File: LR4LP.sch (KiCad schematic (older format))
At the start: 15 parts

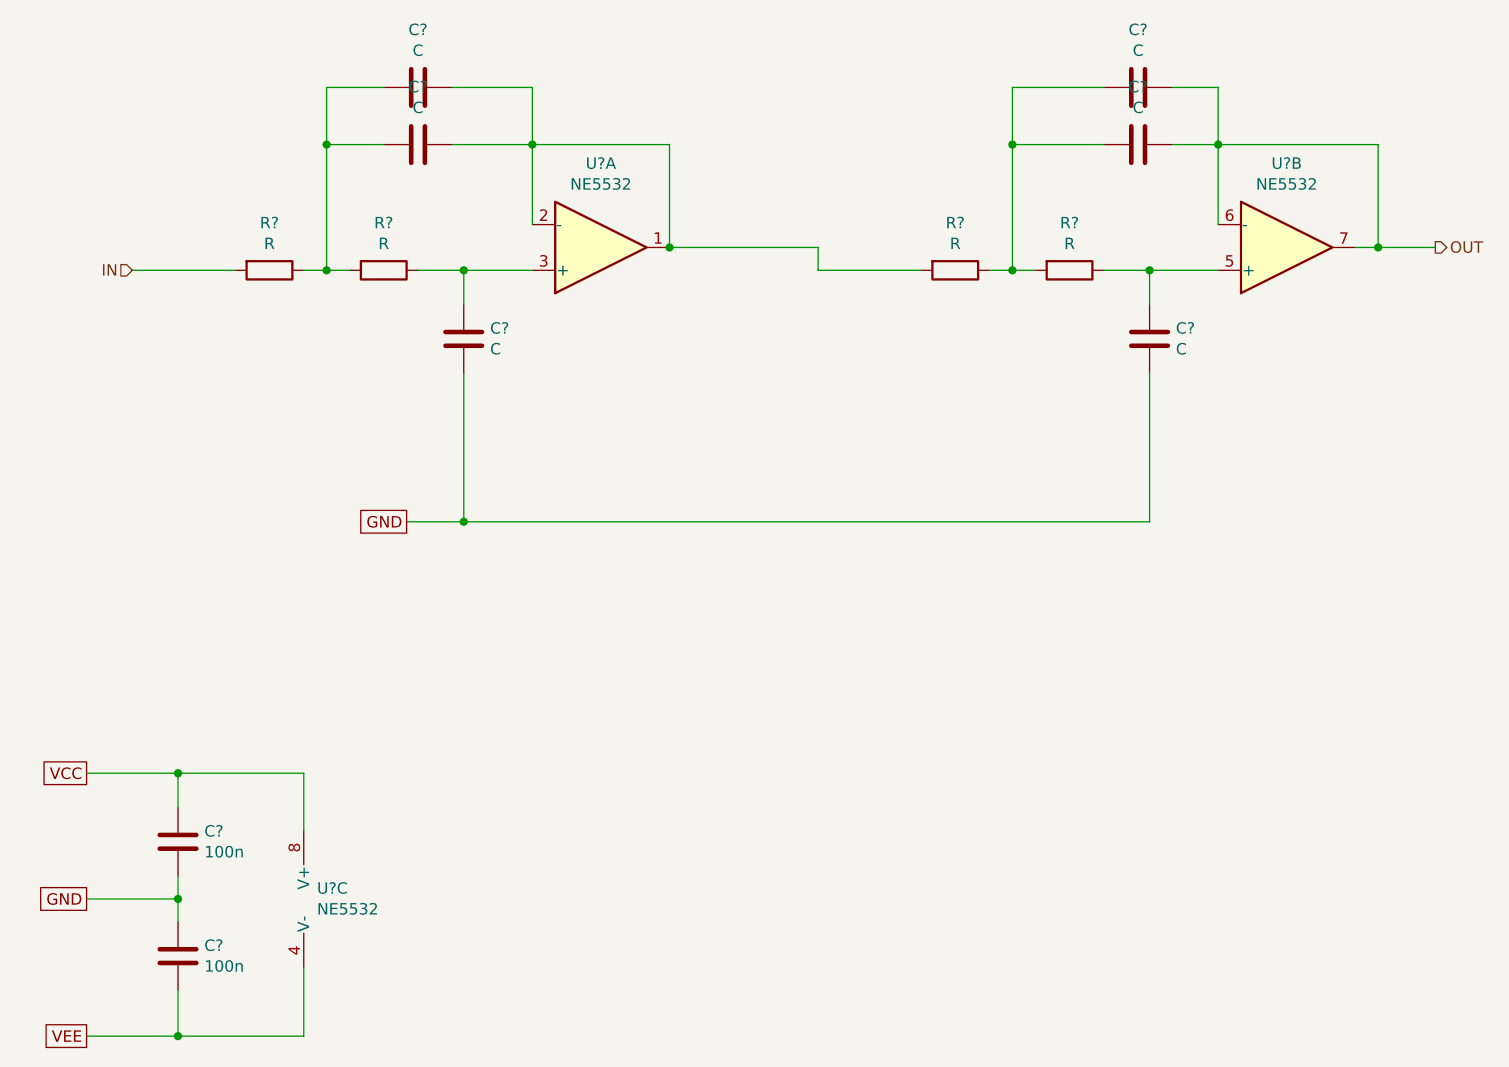
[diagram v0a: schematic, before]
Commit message: improved PSU, gain up front, reordered filter stages, shrunk rumble filter
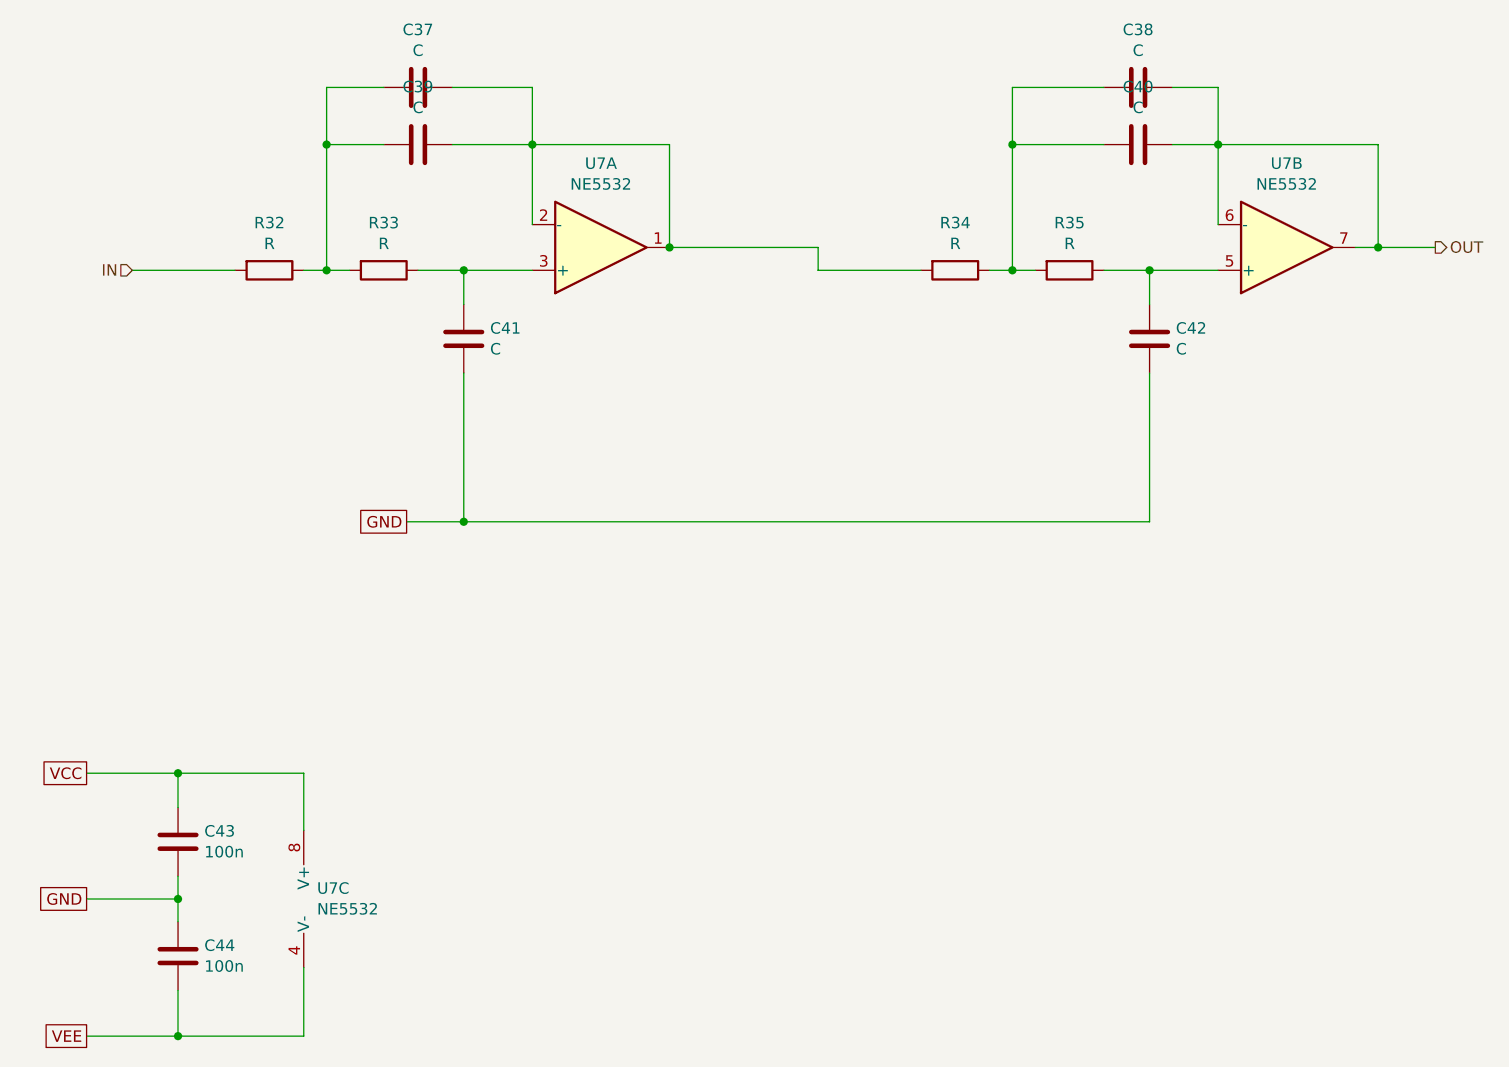
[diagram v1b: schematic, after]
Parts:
- gave numbers to parts that had none: 13
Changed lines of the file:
@@
 AR Path="/615EA975" Ref="U?"  Part="3"
 AR Path="/6157B871/615EA975" Ref="U?"  Part="3"
-AR Path="/615E7263/615EA975" Ref="U?"  Part="3"
-AR Path="/615961F5/615EA975" Ref="U?"  Part="3"
+AR Path="/615E7263/615EA975" Ref="U2"  Part="3"
+AR Path="/615961F5/615EA975" Ref="U4"  Part="3"
 AR Path="/61596D2E/615EA975" Ref="U?"  Part="3"
 AR Path="/61597705/615EA975" Ref="U?"  Part="3"
-AR Path="/615C4B58/615EA975" Ref="U?"  Part="3"
-F 0 "U?" H 3608 5246 50  0000 L CNN
+AR Path="/615C4B58/615EA975" Ref="U7"  Part="3"
+F 0 "U7" H 3608 5246 50  0000 L CNN
 F 1 "NE5532" H 3608 5155 50  0000 L CNN
 F 2 "Housings_DIP:DIP-8_W7.62mm_Socket" H 3650 5200 50  0001 C CNN
@@
 P 3000 5450
 AR Path="/6157B871/615EA97C" Ref="C?"  Part="1"
-AR Path="/615E7263/615EA97C" Ref="C?"  Part="1"
-AR Path="/615961F5/615EA97C" Ref="C?"  Part="1"
+AR Path="/615E7263/615EA97C" Ref="C12"  Part="1"
+AR Path="/615961F5/615EA97C" Ref="C26"  Part="1"
 AR Path="/61596D2E/615EA97C" Ref="C?"  Part="1"
 AR Path="/61597705/615EA97C" Ref="C?"  Part="1"
-AR Path="/615C4B58/615EA97C" Ref="C?"  Part="1"
-F 0 "C?" H 3115 5496 50  0000 L CNN
+AR Path="/615C4B58/615EA97C" Ref="C44"  Part="1"
+F 0 "C44" H 3115 5496 50  0000 L CNN
 F 1 "100n" H 3115 5405 50  0000 L CNN
 F 2 "Capacitors_SMD:C_0805" H 3038 5300 50  0001 C CNN
@@
 P 3400 2450
 AR Path="/6157B871/615EA996" Ref="R?"  Part="1"
-AR Path="/615E7263/615EA996" Ref="R?"  Part="1"
-AR Path="/615961F5/615EA996" Ref="R?"  Part="1"
+AR Path="/615E7263/615EA996" Ref="R8"  Part="1"
+AR Path="/615961F5/615EA996" Ref="R18"  Part="1"
 AR Path="/61596D2E/615EA996" Ref="R?"  Part="1"
 AR Path="/61597705/615EA996" Ref="R?"  Part="1"
-AR Path="/615C4B58/615EA996" Ref="R?"  Part="1"
-F 0 "R?" V 3193 2450 50  0000 C CNN
+AR Path="/615C4B58/615EA996" Ref="R32"  Part="1"
+F 0 "R32" V 3193 2450 50  0000 C CNN
 F 1 "R" V 3284 2450 50  0000 C CNN
 F 2 "Resistors_SMD:R_0805" V 3330 2450 50  0001 C CNN
@@
 P 3900 2450
 AR Path="/6157B871/615EA99C" Ref="R?"  Part="1"
-AR Path="/615E7263/615EA99C" Ref="R?"  Part="1"
-AR Path="/615961F5/615EA99C" Ref="R?"  Part="1"
+AR Path="/615E7263/615EA99C" Ref="R9"  Part="1"
+AR Path="/615961F5/615EA99C" Ref="R19"  Part="1"
 AR Path="/61596D2E/615EA99C" Ref="R?"  Part="1"
 AR Path="/61597705/615EA99C" Ref="R?"  Part="1"
-AR Path="/615C4B58/615EA99C" Ref="R?"  Part="1"
-F 0 "R?" V 3693 2450 50  0000 C CNN
+AR Path="/615C4B58/615EA99C" Ref="R33"  Part="1"
+F 0 "R33" V 3693 2450 50  0000 C CNN
 F 1 "R" V 3784 2450 50  0000 C CNN
 F 2 "Resistors_SMD:R_0805" V 3830 2450 50  0001 C CNN
@@
 P 4050 1900
 AR Path="/6157B871/615EA9A2" Ref="C?"  Part="1"
-AR Path="/615E7263/615EA9A2" Ref="C?"  Part="1"
-AR Path="/615961F5/615EA9A2" Ref="C?"  Part="1"
+AR Path="/615E7263/615EA9A2" Ref="C7"  Part="1"
+AR Path="/615961F5/615EA9A2" Ref="C21"  Part="1"
 AR Path="/61596D2E/615EA9A2" Ref="C?"  Part="1"
 AR Path="/61597705/615EA9A2" Ref="C?"  Part="1"
-AR Path="/615C4B58/615EA9A2" Ref="C?"  Part="1"
-F 0 "C?" V 3798 1900 50  0000 C CNN
+AR Path="/615C4B58/615EA9A2" Ref="C39"  Part="1"
+F 0 "C39" V 3798 1900 50  0000 C CNN
 F 1 "C" V 3889 1900 50  0000 C CNN
 F 2 "Capacitors_SMD:C_1210_HandSoldering" H 4088 1750 50  0001 C CNN
@@
 P 4250 2750
 AR Path="/6157B871/615EA9A8" Ref="C?"  Part="1"
-AR Path="/615E7263/615EA9A8" Ref="C?"  Part="1"
-AR Path="/615961F5/615EA9A8" Ref="C?"  Part="1"
+AR Path="/615E7263/615EA9A8" Ref="C9"  Part="1"
+AR Path="/615961F5/615EA9A8" Ref="C23"  Part="1"
 AR Path="/61596D2E/615EA9A8" Ref="C?"  Part="1"
 AR Path="/61597705/615EA9A8" Ref="C?"  Part="1"
-AR Path="/615C4B58/615EA9A8" Ref="C?"  Part="1"
-F 0 "C?" H 4135 2704 50  0000 R CNN
+AR Path="/615C4B58/615EA9A8" Ref="C41"  Part="1"
+F 0 "C41" H 4135 2704 50  0000 R CNN
 F 1 "C" H 4135 2795 50  0000 R CNN
 F 2 "Capacitors_SMD:C_1210_HandSoldering" H 4288 2600 50  0001 C CNN
@@
 AR Path="/615EA9B4" Ref="U?"  Part="2"
 AR Path="/6157B871/615EA9B4" Ref="U?"  Part="2"
-AR Path="/615E7263/615EA9B4" Ref="U?"  Part="2"
-AR Path="/615961F5/615EA9B4" Ref="U?"  Part="2"
+AR Path="/615E7263/615EA9B4" Ref="U2"  Part="2"
+AR Path="/615961F5/615EA9B4" Ref="U4"  Part="2"
 AR Path="/61596D2E/615EA9B4" Ref="U?"  Part="2"
 AR Path="/61597705/615EA9B4" Ref="U?"  Part="2"
-AR Path="/615C4B58/615EA9B4" Ref="U?"  Part="2"
-F 0 "U?" H 7850 1983 50  0000 C CNN
+AR Path="/615C4B58/615EA9B4" Ref="U7"  Part="2"
+F 0 "U7" H 7850 1983 50  0000 C CNN
 F 1 "NE5532" H 7850 2074 50  0000 C CNN
 F 2 "Housings_DIP:DIP-8_W7.62mm_Socket" H 7850 2350 50  0001 C CNN
@@
 P 3000 4950
 AR Path="/6157B871/615EA9EC" Ref="C?"  Part="1"
-AR Path="/615E7263/615EA9EC" Ref="C?"  Part="1"
-AR Path="/615961F5/615EA9EC" Ref="C?"  Part="1"
+AR Path="/615E7263/615EA9EC" Ref="C11"  Part="1"
+AR Path="/615961F5/615EA9EC" Ref="C25"  Part="1"
 AR Path="/61596D2E/615EA9EC" Ref="C?"  Part="1"
 AR Path="/61597705/615EA9EC" Ref="C?"  Part="1"
-AR Path="/615C4B58/615EA9EC" Ref="C?"  Part="1"
-F 0 "C?" H 3115 4996 50  0000 L CNN
+AR Path="/615C4B58/615EA9EC" Ref="C43"  Part="1"
+F 0 "C43" H 3115 4996 50  0000 L CNN
 F 1 "100n" H 3115 4905 50  0000 L CNN
 F 2 "Capacitors_SMD:C_0805" H 3038 4800 50  0001 C CNN
@@
 AR Path="/615EA9AE" Ref="U?"  Part="1"
 AR Path="/6157B871/615EA9AE" Ref="U?"  Part="1"
-AR Path="/615E7263/615EA9AE" Ref="U?"  Part="1"
-AR Path="/615961F5/615EA9AE" Ref="U?"  Part="1"
+AR Path="/615E7263/615EA9AE" Ref="U2"  Part="1"
+AR Path="/615961F5/615EA9AE" Ref="U4"  Part="1"
 AR Path="/61596D2E/615EA9AE" Ref="U?"  Part="1"
 AR Path="/61597705/615EA9AE" Ref="U?"  Part="1"
-AR Path="/615C4B58/615EA9AE" Ref="U?"  Part="1"
-F 0 "U?" H 4850 1983 50  0000 C CNN
+AR Path="/615C4B58/615EA9AE" Ref="U7"  Part="1"
+F 0 "U7" H 4850 1983 50  0000 C CNN
 F 1 "NE5532" H 4850 2074 50  0000 C CNN
 F 2 "Housings_DIP:DIP-8_W7.62mm_Socket" H 4850 2350 50  0001 C CNN
@@
 P 4050 1650
 AR Path="/6157B871/6160176B" Ref="C?"  Part="1"
-AR Path="/615E7263/6160176B" Ref="C?"  Part="1"
-AR Path="/615961F5/6160176B" Ref="C?"  Part="1"
+AR Path="/615E7263/6160176B" Ref="C5"  Part="1"
+AR Path="/615961F5/6160176B" Ref="C19"  Part="1"
 AR Path="/61596D2E/6160176B" Ref="C?"  Part="1"
 AR Path="/61597705/6160176B" Ref="C?"  Part="1"
-AR Path="/615C4B58/6160176B" Ref="C?"  Part="1"
-F 0 "C?" V 3798 1650 50  0000 C CNN
+AR Path="/615C4B58/6160176B" Ref="C37"  Part="1"
+F 0 "C37" V 3798 1650 50  0000 C CNN
 F 1 "C" V 3889 1650 50  0000 C CNN
 F 2 "Capacitors_SMD:C_1210_HandSoldering" H 4088 1500 50  0001 C CNN
@@
 P 6400 2450
 AR Path="/6157B871/61611E6C" Ref="R?"  Part="1"
-AR Path="/615E7263/61611E6C" Ref="R?"  Part="1"
-AR Path="/615961F5/61611E6C" Ref="R?"  Part="1"
+AR Path="/615E7263/61611E6C" Ref="R10"  Part="1"
+AR Path="/615961F5/61611E6C" Ref="R20"  Part="1"
 AR Path="/61596D2E/61611E6C" Ref="R?"  Part="1"
 AR Path="/61597705/61611E6C" Ref="R?"  Part="1"
-AR Path="/615C4B58/61611E6C" Ref="R?"  Part="1"
-F 0 "R?" V 6193 2450 50  0000 C CNN
+AR Path="/615C4B58/61611E6C" Ref="R34"  Part="1"
+F 0 "R34" V 6193 2450 50  0000 C CNN
 F 1 "R" V 6284 2450 50  0000 C CNN
 F 2 "Resistors_SMD:R_0805" V 6330 2450 50  0001 C CNN
@@
 P 6900 2450
 AR Path="/6157B871/61611E72" Ref="R?"  Part="1"
-AR Path="/615E7263/61611E72" Ref="R?"  Part="1"
-AR Path="/615961F5/61611E72" Ref="R?"  Part="1"
+AR Path="/615E7263/61611E72" Ref="R11"  Part="1"
+AR Path="/615961F5/61611E72" Ref="R21"  Part="1"
 AR Path="/61596D2E/61611E72" Ref="R?"  Part="1"
 AR Path="/61597705/61611E72" Ref="R?"  Part="1"
-AR Path="/615C4B58/61611E72" Ref="R?"  Part="1"
-F 0 "R?" V 6693 2450 50  0000 C CNN
+AR Path="/615C4B58/61611E72" Ref="R35"  Part="1"
+F 0 "R35" V 6693 2450 50  0000 C CNN
 F 1 "R" V 6784 2450 50  0000 C CNN
 F 2 "Resistors_SMD:R_0805" V 6830 2450 50  0001 C CNN
@@
 P 7200 1900
 AR Path="/6157B871/61611E78" Ref="C?"  Part="1"
-AR Path="/615E7263/61611E78" Ref="C?"  Part="1"
-AR Path="/615961F5/61611E78" Ref="C?"  Part="1"
+AR Path="/615E7263/61611E78" Ref="C8"  Part="1"
+AR Path="/615961F5/61611E78" Ref="C22"  Part="1"
 AR Path="/61596D2E/61611E78" Ref="C?"  Part="1"
 AR Path="/61597705/61611E78" Ref="C?"  Part="1"
-AR Path="/615C4B58/61611E78" Ref="C?"  Part="1"
-F 0 "C?" V 6948 1900 50  0000 C CNN
+AR Path="/615C4B58/61611E78" Ref="C40"  Part="1"
+F 0 "C40" V 6948 1900 50  0000 C CNN
 F 1 "C" V 7039 1900 50  0000 C CNN
 F 2 "Capacitors_SMD:C_1210_HandSoldering" H 7238 1750 50  0001 C CNN
@@
 P 7250 2750
 AR Path="/6157B871/61611E7E" Ref="C?"  Part="1"
-AR Path="/615E7263/61611E7E" Ref="C?"  Part="1"
-AR Path="/615961F5/61611E7E" Ref="C?"  Part="1"
+AR Path="/615E7263/61611E7E" Ref="C10"  Part="1"
+AR Path="/615961F5/61611E7E" Ref="C24"  Part="1"
 AR Path="/61596D2E/61611E7E" Ref="C?"  Part="1"
 AR Path="/61597705/61611E7E" Ref="C?"  Part="1"
-AR Path="/615C4B58/61611E7E" Ref="C?"  Part="1"
-F 0 "C?" H 7135 2704 50  0000 R CNN
+AR Path="/615C4B58/61611E7E" Ref="C42"  Part="1"
+F 0 "C42" H 7135 2704 50  0000 R CNN
 F 1 "C" H 7135 2795 50  0000 R CNN
 F 2 "Capacitors_SMD:C_1210_HandSoldering" H 7288 2600 50  0001 C CNN
@@
 P 7200 1650
 AR Path="/6157B871/61611E88" Ref="C?"  Part="1"
-AR Path="/615E7263/61611E88" Ref="C?"  Part="1"
-AR Path="/615961F5/61611E88" Ref="C?"  Part="1"
+AR Path="/615E7263/61611E88" Ref="C6"  Part="1"
+AR Path="/615961F5/61611E88" Ref="C20"  Part="1"
 AR Path="/61596D2E/61611E88" Ref="C?"  Part="1"
 AR Path="/61597705/61611E88" Ref="C?"  Part="1"
-AR Path="/615C4B58/61611E88" Ref="C?"  Part="1"
-F 0 "C?" V 6948 1650 50  0000 C CNN
+AR Path="/615C4B58/61611E88" Ref="C38"  Part="1"
+F 0 "C38" V 6948 1650 50  0000 C CNN
 F 1 "C" V 7039 1650 50  0000 C CNN
 F 2 "Capacitors_SMD:C_1210_HandSoldering" H 7238 1500 50  0001 C CNN
